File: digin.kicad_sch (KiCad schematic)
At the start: 16 parts, among them U10 ADUM5242ARZ, U21 ADUM5242ARZ, U25 TXUN0104RUTR

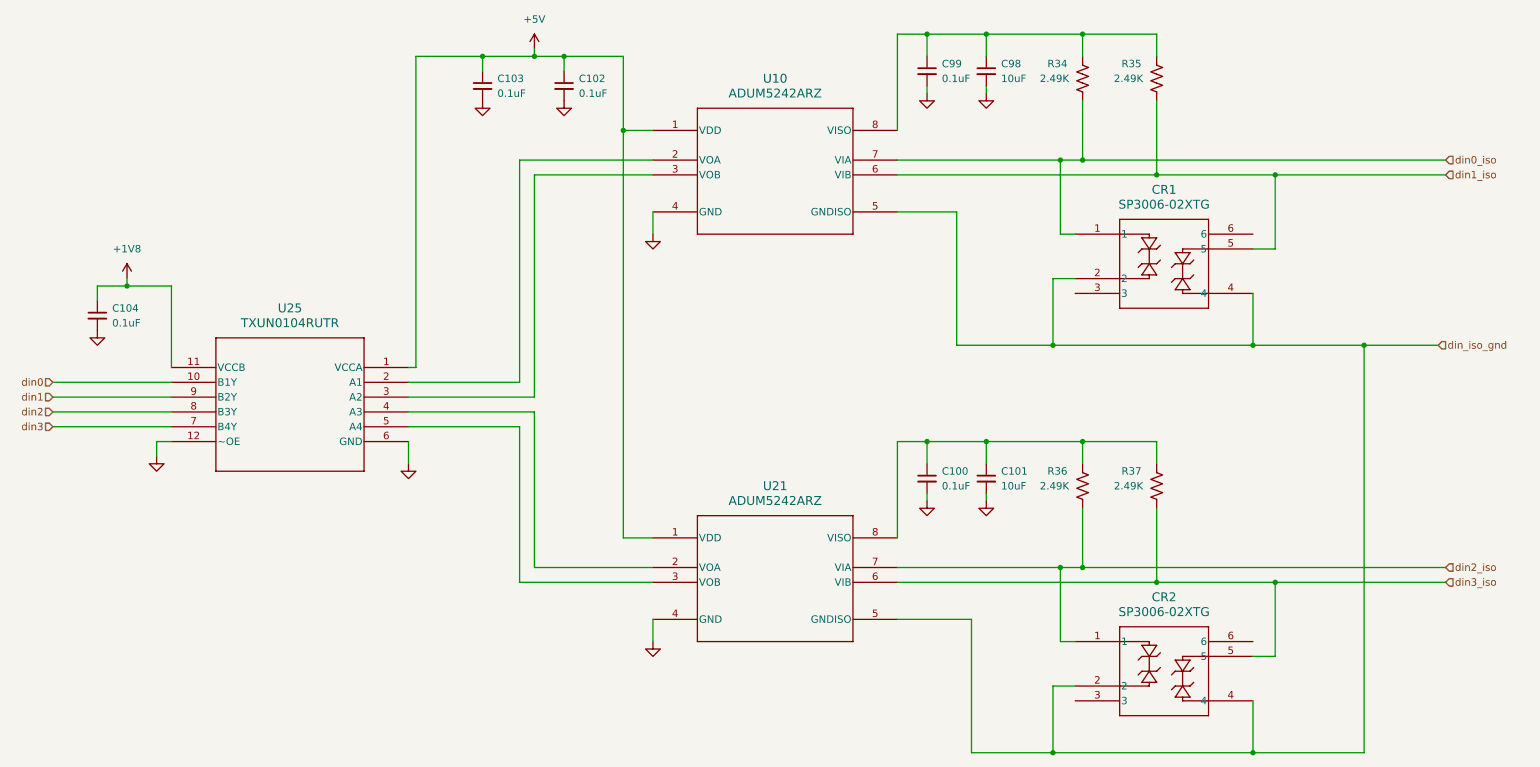
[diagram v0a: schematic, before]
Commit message: Add DCCT ADCs
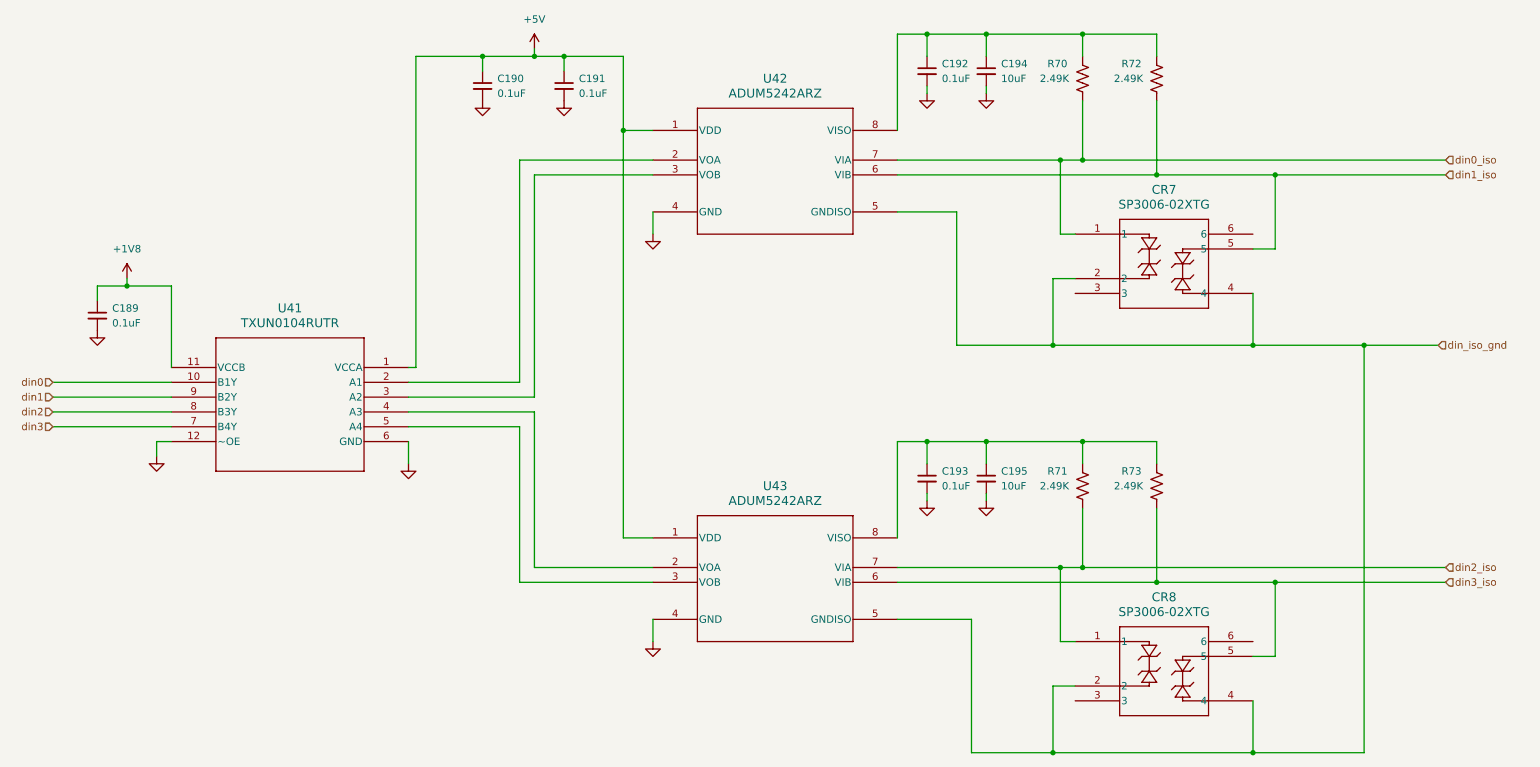
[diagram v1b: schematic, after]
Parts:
- U42: renamed from U10; footprint myparts:R_8_ADI-M -> myparts:R_8_ADI
- U43: renamed from U21; footprint myparts:R_8_ADI-M -> myparts:R_8_ADI
- renumbered C104 to C189, C103 to C190, C102 to C191, C99 to C192, C100 to C193, C98 to C194, C101 to C195, CR1 to CR7, CR2 to CR8, R34 to R70, R36 to R71, R35 to R72, R37 to R73, U25 to U41

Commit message: Finish layout
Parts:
- added C102: 0.1uF, Capacitor_SMD:C_0402_1005Metric, symbol Device:C_Small
- C189, C190, C191, C192, C193: MFG (none) -> Taiyo Yuden; MFG_PN (none) -> TMK105BJ104KV-F
- C194, C195: MFG (none) -> Samsung; MFG_PN (none) -> CL10A106MA8NRNC
- CR7, CR8: Cost (none) -> 0.65; MFG (none) -> Littlefuse; MFG_PN (none) -> SP3006-02XTG
- R70, R71, R72, R73: Cost (none) -> .01; MFG (none) -> Panasonic; MFG_PN (none) -> ERJ-2RKF2491X
- U41: Cost (none) -> .77; MFG (none) -> TI; MFG_PN (none) -> TXUN0104RUTR
- U42, U43: footprint myparts:R_8_ADI -> myparts:R_8_ADI-M; Cost (none) -> 6.81; MFG (none) -> Analog Devices; MFG_PN (none) -> ADUM5242ARZ
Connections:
- net GND: now also C102.2
- net +5V renamed +5.0V
- net +5.0V: now also C102.1
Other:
- moved on the sheet: C190
